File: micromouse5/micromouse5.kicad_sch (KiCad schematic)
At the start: 7 parts, among them J1 Conn_01x06_Pin, J2 Conn_01x06_Pin, U1 HBridge

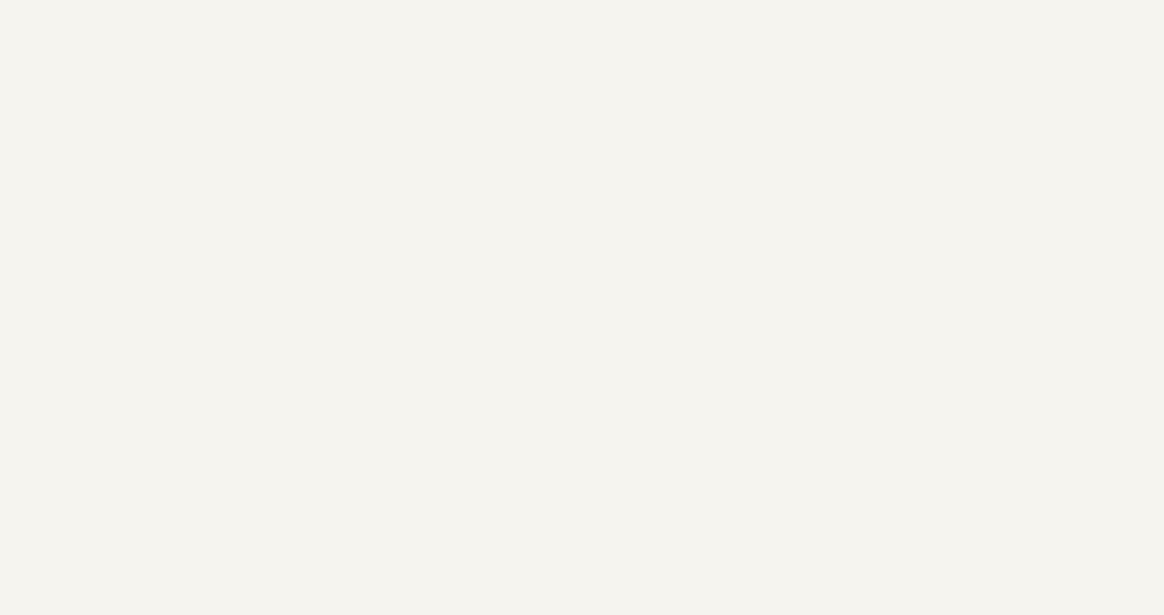
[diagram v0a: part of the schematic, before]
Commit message: added voltage regulator
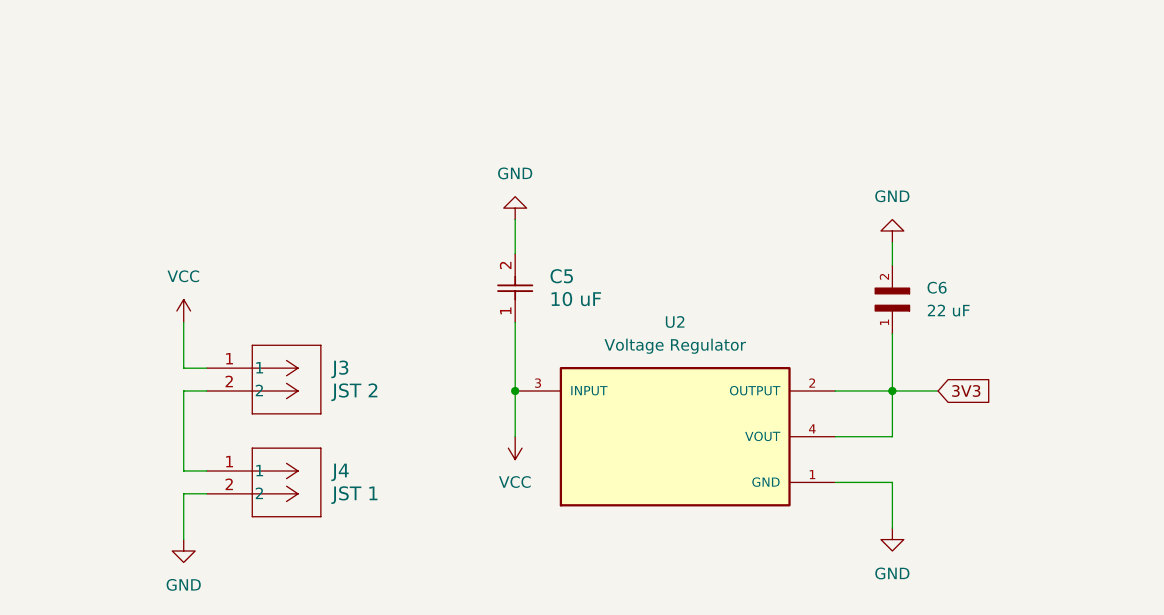
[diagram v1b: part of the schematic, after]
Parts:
- added C5: 10 uF, G-21_MUR, symbol GRM21BR61C106KE15L(10):GRM21BR61C106KE15L
- added C6: 22 uF, GRM21BR61A226ME51L:CAPC2012X140N, symbol GRM21BR61A226ME51L:GRM21BR61A226ME51L
- added J3: JST 2, CONN2_B2B-PH-K-S_JST, symbol B2B_PH_K_S:B2B-PH-K-S
- added J4: JST 1, CONN2_B2B-PH-K-S_JST, symbol B2B_PH_K_S:B2B-PH-K-S
- added U2: Voltage Regulator, AZ1117IH-3.3TRG1:SOT230P700X185-4N, symbol AZ1117IH-3.3TRG1:AZ1117IH-3.3TRG1
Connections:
- net 3V3: now also C6.1, U2.2 (OUTPUT), U2.4 (VOUT)
- net GND: now also C5.2, C6.2, J4.2, U2.1 (GND)
- net VCC: now also C5.1, J3.1, U2.3 (INPUT)
- new net: J3.2, J4.1

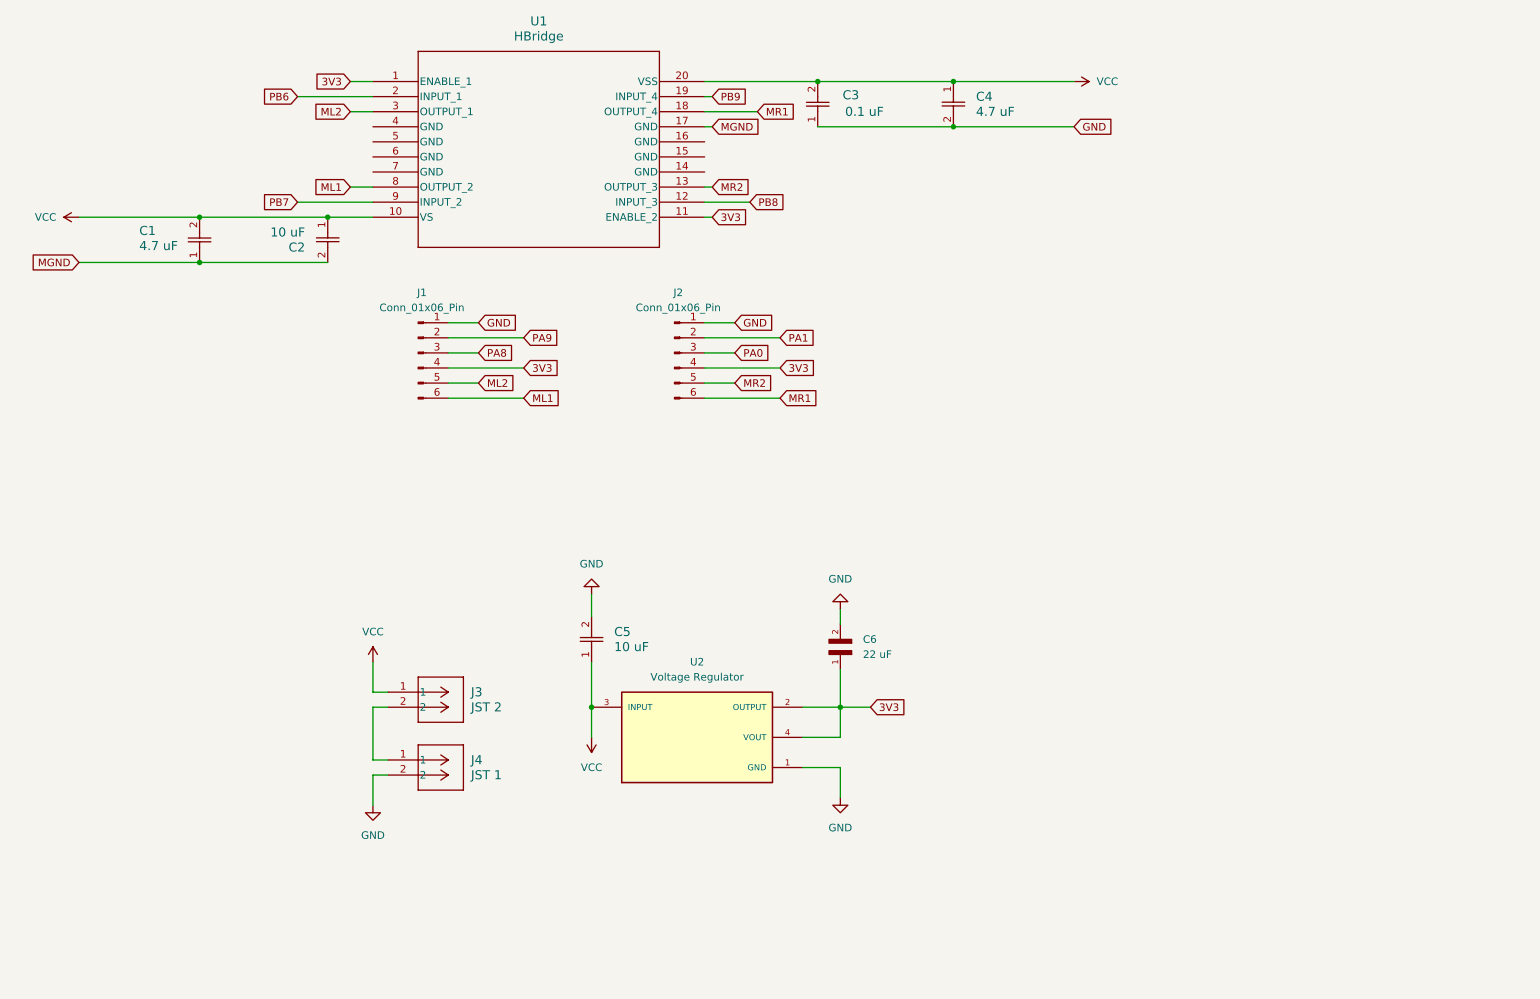
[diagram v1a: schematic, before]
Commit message: Schematic MM
Assignment 5
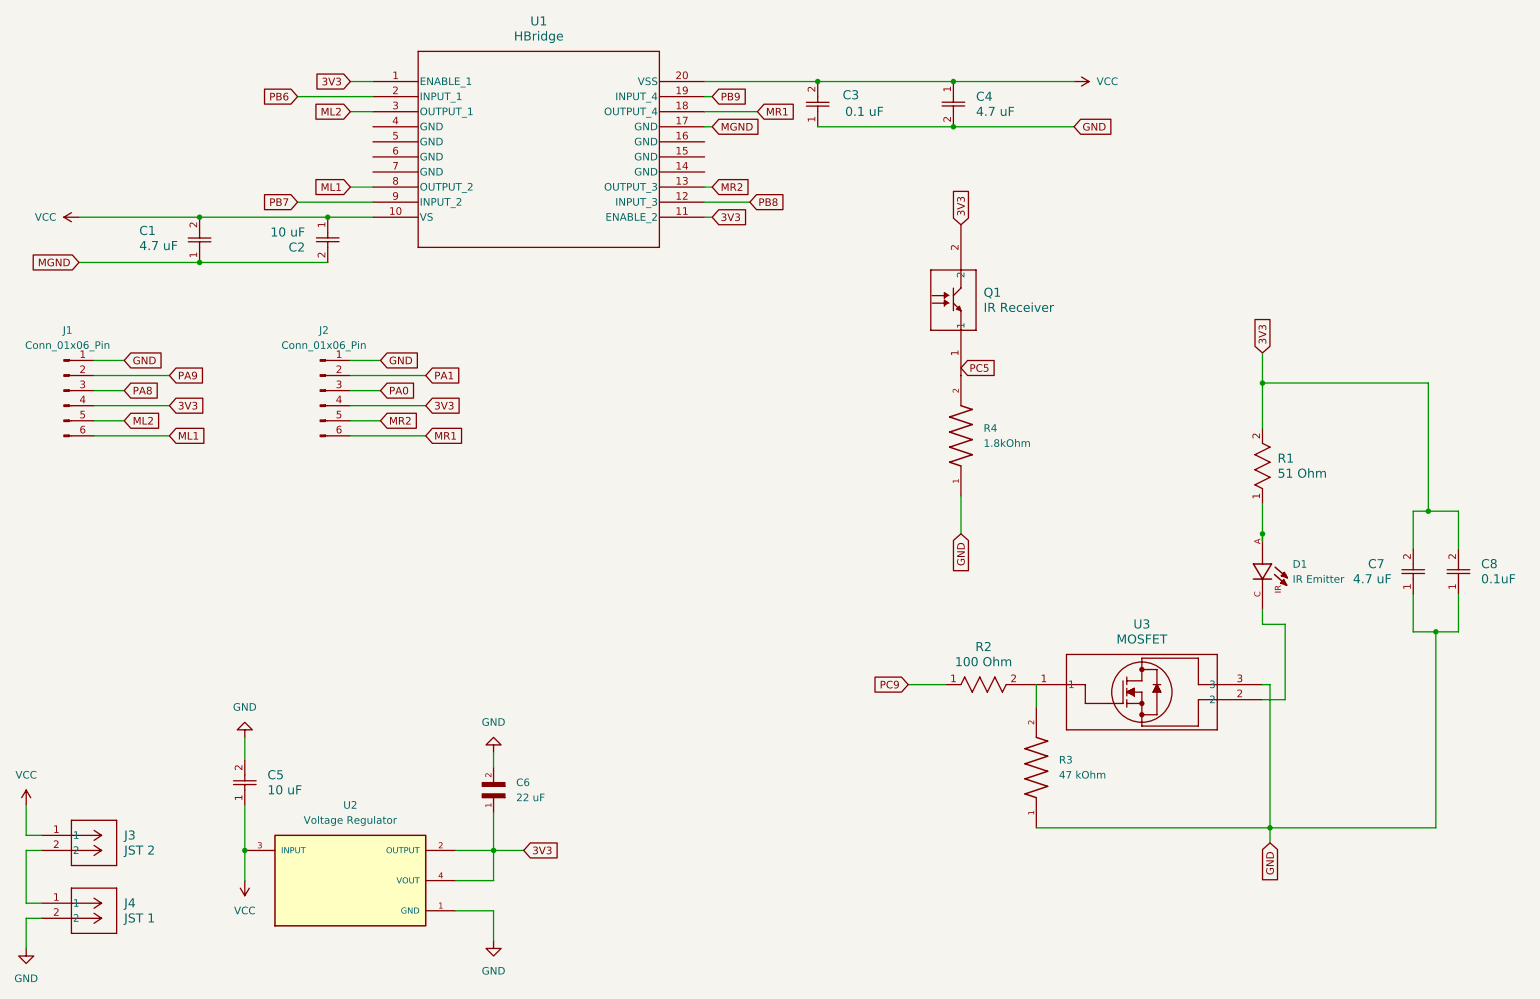
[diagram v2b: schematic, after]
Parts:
- added C7: 4.7 uF, G-21_MUR, symbol Capacitor-4.7uF:GCJ21BR72A104KA01L
- added C8: 0.1uF, CAP_GRM0805_2X1P25_MUR, symbol Capacitor-0.1uF:GRM21BR71C475KE51L
- added D1: IR Emitter, SFH_4545:DIO_SFH_4545, symbol IR-Emitter:SFH_4545
- added Q1: IR Receiver, NoneP157X157-2_LTO, symbol IR-Receiver:LTR-4206E
- added R1: 51 Ohm, BO_CR0805, symbol Resistor- 51ohm:CRM0805-FX-51R0ELF
- added R2: 100 Ohm, STA_RNCP0805_STP, symbol Resistor- 100ohm:RNCP0805FTD100R
- added R3: 47 kOhm, RK73H2ARTTD4702F:RESC2012X60N, symbol Resistor- 47kohm:RK73H2ARTTD4702F
- added R4: 1.8kOhm, RK73H2ATTD1801F:RESC2012X60N, symbol Resistor- 1.8kohm:RK73H2ATTD1801F
- added U3: MOSFET, SOT-23_3L_ONS, symbol Mosfet:2N7002LT1G
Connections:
- net 3V3: now also C7.2, C8.2, Q1.2, R1.2
- net GND: now also C7.1, C8.1, R3.1, R4.1, U3.3
- new net: R2.2, U3.1
- new net: D1.C, U3.2
- new net: D1.A, R1.1
- new net: Q1.1, R4.2
- new net PC9: R2.1
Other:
- moved on the sheet: C5, C6, J1, J2, J3, J4, U2

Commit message: Trying to commit footprints
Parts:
- C1, C4, C8: footprint CAP_GRM0805_2X1P25_MUR -> Capacitor-0.1uF:CAP_GRM0805_2X1P25_MUR
- Q1: footprint NoneP157X157-2_LTO -> IR- Receiver:NoneP157X157-2_LTO
- U3: footprint SOT-23_3L_ONS -> Mosfet:SOT-23_3L_ONS
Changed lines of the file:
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@@
 			)
 		)
-		(property "Footprint" "SOT-23_3L_ONS"
+		(property "Footprint" "Mosfet:SOT-23_3L_ONS"
 			(at 196.85 128.27 0)
 			(effects
@@
 			)
 		)
-		(property "Footprint" "CAP_GRM0805_2X1P25_MUR"
+		(property "Footprint" "Capacitor-0.1uF:CAP_GRM0805_2X1P25_MUR"
 			(at 185.42 26.67 0)
 			(effects
@@
 			)
 		)
-		(property "Footprint" "CAP_GRM0805_2X1P25_MUR"
+		(property "Footprint" "Capacitor-0.1uF:CAP_GRM0805_2X1P25_MUR"
 			(at 270.51 113.03 0)
 			(effects
@@
 			)
 		)
-		(property "Footprint" "CAP_GRM0805_2X1P25_MUR"
+		(property "Footprint" "Capacitor-0.1uF:CAP_GRM0805_2X1P25_MUR"
 			(at 58.42 57.15 0)
 			(effects
@@
 			)
 		)
-		(property "Footprint" "NoneP157X157-2_LTO"
+		(property "Footprint" "IR- Receiver:NoneP157X157-2_LTO"
 			(at 186.69 76.2 0)
 			(effects

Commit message: updated footprint associations
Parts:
- C1, C4: footprint Capacitor-0.1uF:CAP_GRM0805_2X1P25_MUR -> micromouse5:CAP_GRM0805_2X1P25_MUR
- C2: footprint G-21_MUR -> micromouse5:G-21_MUR(0.1)
- C3, C5: footprint G-21_MUR -> micromouse5:G-21_MUR(10)
- C6: footprint GRM21BR61A226ME51L:CAPC2012X140N -> micromouse5:CAPC2012X140N
- C7: footprint G-21_MUR -> micromouse5:CAP_GRM0805_2X1P25_MUR
- C8: footprint Capacitor-0.1uF:CAP_GRM0805_2X1P25_MUR -> micromouse5:G-21_MUR(0.1)
- U1: footprint SO-20_STM -> micromouse5:SO-20_STM
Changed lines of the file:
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@@
 			)
 		)
-		(property "Footprint" "Capacitor-0.1uF:CAP_GRM0805_2X1P25_MUR"
+		(property "Footprint" "micromouse5:CAP_GRM0805_2X1P25_MUR"
 			(at 185.42 26.67 0)
 			(effects
@@
 			)
 		)
-		(property "Footprint" "G-21_MUR"
+		(property "Footprint" "micromouse5:G-21_MUR(10)"
 			(at 66.04 148.59 0)
 			(effects
@@
 			)
 		)
-		(property "Footprint" "Capacitor-0.1uF:CAP_GRM0805_2X1P25_MUR"
+		(property "Footprint" "micromouse5:G-21_MUR(0.1)"
 			(at 270.51 113.03 0)
 			(effects
@@
 			)
 		)
-		(property "Footprint" "GRM21BR61A226ME51L:CAPC2012X140N"
+		(property "Footprint" "micromouse5:CAPC2012X140N"
 			(at 107.95 147.32 0)
 			(effects
@@
 			)
 		)
-		(property "Footprint" "Capacitor-0.1uF:CAP_GRM0805_2X1P25_MUR"
+		(property "Footprint" "micromouse5:CAP_GRM0805_2X1P25_MUR"
 			(at 58.42 57.15 0)
 			(effects
@@
 			)
 		)
-		(property "Footprint" "G-21_MUR"
+		(property "Footprint" "micromouse5:G-21_MUR(10)"
 			(at 162.56 34.29 0)
 			(effects
@@
 			)
 		)
-		(property "Footprint" "SO-20_STM"
+		(property "Footprint" "micromouse5:SO-20_STM"
 			(at 87.63 26.67 0)
 			(effects
@@
 			)
 		)
-		(property "Footprint" "G-21_MUR"
+		(property "Footprint" "micromouse5:G-21_MUR(0.1)"
 			(at 80.01 49.53 0)
 			(effects
@@
 			)
 		)
-		(property "Footprint" "G-21_MUR"
+		(property "Footprint" "micromouse5:CAP_GRM0805_2X1P25_MUR"
 			(at 262.89 113.03 0)
 			(effects

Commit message: More associations
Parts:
- D1: footprint SFH_4545:DIO_SFH_4545 -> micromouse5:DIO_SFH_4545 (IR- Emitter)
- J3, J4: footprint CONN2_B2B-PH-K-S_JST -> (none)
- Q1: footprint IR- Receiver:NoneP157X157-2_LTO -> micromouse5:NoneP157X157-2_LTO (IR- Receiver)
- R1: footprint BO_CR0805 -> (none)
- R2: footprint STA_RNCP0805_STP -> (none)
- R3: footprint RK73H2ARTTD4702F:RESC2012X60N -> micromouse5:RESC2012X60N (47kΩ)
- R4: footprint RK73H2ATTD1801F:RESC2012X60N -> micromouse5:RESC2012X60N (1.8kΩ)
- U3: footprint Mosfet:SOT-23_3L_ONS -> micromouse5:SOT-23_3L_ONS (mosfet)
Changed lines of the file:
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@@
 			)
 		)
-		(property "Footprint" "Mosfet:SOT-23_3L_ONS"
+		(property "Footprint" "micromouse5:SOT-23_3L_ONS (mosfet)"
 			(at 196.85 128.27 0)
 			(effects
@@
 			)
 		)
-		(property "Footprint" "SFH_4545:DIO_SFH_4545"
+		(property "Footprint" "micromouse5:DIO_SFH_4545 (IR- Emitter)"
 			(at 237.49 110.49 0)
 			(effects
@@
 			)
 		)
-		(property "Footprint" "CONN2_B2B-PH-K-S_JST"
+		(property "Footprint" ""
 			(at 31.75 165.1 0)
 			(effects
@@
 			)
 		)
-		(property "Footprint" "BO_CR0805"
+		(property "Footprint" ""
 			(at 237.49 97.79 0)
 			(effects
@@
 			)
 		)
-		(property "Footprint" "RK73H2ARTTD4702F:RESC2012X60N"
+		(property "Footprint" "micromouse5:RESC2012X60N (47kΩ)"
 			(at 199.39 142.24 0)
 			(effects
@@
 			)
 		)
-		(property "Footprint" "IR- Receiver:NoneP157X157-2_LTO"
+		(property "Footprint" "micromouse5:NoneP157X157-2_LTO (IR- Receiver)"
 			(at 186.69 76.2 0)
 			(effects
@@
 			)
 		)
-		(property "Footprint" "RK73H2ATTD1801F:RESC2012X60N"
+		(property "Footprint" "micromouse5:RESC2012X60N (1.8kΩ)"
 			(at 186.69 86.36 0)
 			(effects
@@
 			)
 		)
-		(property "Footprint" "CONN2_B2B-PH-K-S_JST"
+		(property "Footprint" ""
 			(at 31.75 153.67 0)
 			(effects
@@
 			)
 		)
-		(property "Footprint" "STA_RNCP0805_STP"
+		(property "Footprint" ""
 			(at 184.15 128.27 0)
 			(effects

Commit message: Another association
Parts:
- U2: footprint AZ1117IH-3.3TRG1:SOT230P700X185-4N -> micromouse5:SOT230P700X185-4N
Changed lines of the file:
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@@
 			)
 		)
-		(property "Footprint" "AZ1117IH-3.3TRG1:SOT230P700X185-4N"
+		(property "Footprint" "micromouse5:SOT230P700X185-4N"
 			(at 83.82 161.29 0)
 			(effects

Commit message: missing resistor associations
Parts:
- removed R2: 100 Ohm, symbol Resistor- 100ohm:RNCP0805FTD100R
- added R2: 100 Ohm, micromouse5:STA_RNCP0805_STP(100 ohm), symbol RNCP0805FTD100R(100 resistor):RNCP0805FTD100R
- J3, J4: footprint (none) -> micromouse5:CONN2_B2B-PH-K-S_JST
- R1: footprint (none) -> micromouse5:BO_CR0805
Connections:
- net PC9: now also R2.1
- net at U3.1: now also R2.2
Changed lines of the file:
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@@
 			)
 		)
-		(property "Footprint" ""
+		(property "Footprint" "micromouse5:CONN2_B2B-PH-K-S_JST"
 			(at 31.75 165.1 0)
 			(effects
@@
 	)
 	(symbol
+		(lib_id "RNCP0805FTD100R(100 resistor):RNCP0805FTD100R")
+		(at 184.15 128.27 0)
+		(unit 1)
+		(exclude_from_sim no)
+		(in_bom yes)
+		(on_board yes)
+		(dnp no)
+		(fields_autoplaced yes)
+		(property "Reference" "R2"
+			(at 190.5 121.92 0)
+			(effects
+				(font
+					(size 1.524 1.524)
+				)
+			)
+		)
+		(property "Value" "100 Ohm"
+			(at 190.5 124.46 0)
+			(effects
+				(font
+					(size 1.524 1.524)
+				)
+			)
+		)
+		(property "Footprint" "micromouse5:STA_RNCP0805_STP(100 ohm)"
+			(at 184.15 128.27 0)
+			(effects
+				(font
+					(size 1.27 1.27)
+					(italic yes)
+				)
+				(hide yes)
+			)
+		)
+		(property "Datasheet" "RNCP0805FTD100R"
+			(at 184.15 128.27 0)
+			(effects
+				(font
+					(size 1.27 1.27)
+					(italic yes)
+				)
+				(hide yes)
+			)
+		)
+		(property "Description" ""
+			(at 184.15 128.27 0)
+			(effects
+				(font
+					(size 1.27 1.27)
+				)
+				(hide yes)
+			)
+		)
+		(pin "1"
+		)
+		(pin "2"
+		)
+		(instances
+			(project ""
+				(path "/afbe2d40-4a52-44ad-a632-ed06745a7c8a"
+					(reference "R2")
+					(unit 1)
+				)
+			)
+		)
+	)
+	(symbol
 		(lib_id "GRM21BR71C475KE51L(4.7):GRM21BR71C475KE51L")
 		(at 58.42 57.15 90)
@@
 			)
 		)
-		(property "Footprint" ""
+		(property "Footprint" "micromouse5:BO_CR0805"
 			(at 237.49 97.79 0)
 			(effects
@@
 			)
 		)
-		(property "Footprint" ""
+		(property "Footprint" "micromouse5:CONN2_B2B-PH-K-S_JST"
 			(at 31.75 153.67 0)
 			(effects
@@
 					(unit 1)
 				)
-			)
-		)
-	)
-	(symbol
-		(lib_id "Resistor- 100ohm:RNCP0805FTD100R")
-		(at 184.15 128.27 0)
-		(unit 1)
-		(exclude_from_sim no)
-		(in_bom yes)
-		(on_board yes)
-		(dnp no)
-		(fields_autoplaced yes)
-		(property "Reference" "R2"
-			(at 190.5 121.92 0)
-			(effects
-				(font
-					(size 1.524 1.524)
-				)
-			)
-		)
-		(property "Value" "100 Ohm"
-			(at 190.5 124.46 0)
-			(effects
-				(font
-					(size 1.524 1.524)
-				)
-			)
-		)
-		(property "Footprint" ""
-			(at 184.15 128.27 0)
-			(effects
-				(font
-					(size 1.27 1.27)
-					(italic yes)
-				)
-				(hide yes)
-			)
-		)
-		(property "Datasheet" "RNCP0805FTD100R"
-			(at 184.15 128.27 0)
-			(effects
-				(font
-					(size 1.27 1.27)
-					(italic yes)
-				)
-				(hide yes)
-			)
-		)
-		(property "Description" ""
-			(at 184.15 128.27 0)
-			(effects
-				(font
-					(size 1.27 1.27)
-				)
-				(hide yes)
-			)
-		)
-		(pin "1"
-		)
-		(pin "2"
-		)
-		(instances
-			(project ""
-				(path "/afbe2d40-4a52-44ad-a632-ed06745a7c8a"
-					(reference "R2")
-					(unit 1)
-				)

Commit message: 51 ohm fix
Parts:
- removed R1: 51 Ohm, micromouse5:BO_CR0805, symbol Resistor- 51ohm:CRM0805-FX-51R0ELF
- added R1: 51 Ohm, micromouse5:BO_CR0805, symbol CRM0805-FX-51R0ELF (51 ohm):CRM0805-FX-51R0ELF
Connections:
- net 3V3: now also R1.2
- net at D1.A: now also R1.1
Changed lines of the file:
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@@
+	)
+	(symbol
+		(lib_id "CRM0805-FX-51R0ELF (51 ohm):CRM0805-FX-51R0ELF")
+		(at 237.49 97.79 90)
+		(unit 1)
+		(exclude_from_sim no)
+		(in_bom yes)
+		(on_board yes)
+		(dnp no)
+		(fields_autoplaced yes)
+		(property "Reference" "R1"
+			(at 240.03 90.1699 90)
+			(effects
+				(font
+					(size 1.524 1.524)
+				)
+				(justify right)
+			)
+		)
+		(property "Value" "51 Ohm"
+			(at 240.03 92.7099 90)
+			(effects
+				(font
+					(size 1.524 1.524)
+				)
+				(justify right)
+			)
+		)
+		(property "Footprint" "micromouse5:BO_CR0805"
+			(at 237.49 97.79 0)
+			(effects
+				(font
+					(size 1.27 1.27)
+					(italic yes)
+				)
+				(hide yes)
+			)
+		)
+		(property "Datasheet" "CRM0805-FX-51R0ELF"
+			(at 237.49 97.79 0)
+			(effects
+				(font
+					(size 1.27 1.27)
+					(italic yes)
+				)
+				(hide yes)
+			)
+		)
+		(property "Description" ""
+			(at 237.49 97.79 0)
+			(effects
+				(font
+					(size 1.27 1.27)
+				)
+				(hide yes)
+			)
+		)
+		(pin "2"
+		)
+		(pin "1"
+		)
+		(instances
+			(project ""
+				(path "/afbe2d40-4a52-44ad-a632-ed06745a7c8a"
+					(reference "R1")
+					(unit 1)
+				)
+			)
+		)
 	)
 	(symbol
@@
 					(unit 1)
 				)
-			)
-		)
-	)
-	(symbol
-		(lib_id "Resistor- 51ohm:CRM0805-FX-51R0ELF")
-		(at 237.49 97.79 90)
-		(unit 1)
-		(exclude_from_sim no)
-		(in_bom yes)
-		(on_board yes)
-		(dnp no)
-		(fields_autoplaced yes)
-		(property "Reference" "R1"
-			(at 240.03 90.1699 90)
-			(effects
-				(font
-					(size 1.524 1.524)
-				)
-				(justify right)
-			)
-		)
-		(property "Value" "51 Ohm"
-			(at 240.03 92.7099 90)
-			(effects
-				(font
-					(size 1.524 1.524)
-				)
-				(justify right)
-			)
-		)
-		(property "Footprint" "micromouse5:BO_CR0805"
-			(at 237.49 97.79 0)
-			(effects
-				(font
-					(size 1.27 1.27)
-					(italic yes)
-				)
-				(hide yes)
-			)
-		)
-		(property "Datasheet" "CRM0805-FX-51R0ELF"
-			(at 237.49 97.79 0)
-			(effects
-				(font
-					(size 1.27 1.27)
-					(italic yes)
-				)
-				(hide yes)
-			)
-		)
-		(property "Description" ""
-			(at 237.49 97.79 0)
-			(effects
-				(font
-					(size 1.27 1.27)
-				)
-				(hide yes)
-			)
-		)
-		(pin "1"
-		)
-		(pin "2"
-		)
-		(instances
-			(project ""
-				(path "/afbe2d40-4a52-44ad-a632-ed06745a7c8a"
-					(reference "R1")
-					(unit 1)
-				)
